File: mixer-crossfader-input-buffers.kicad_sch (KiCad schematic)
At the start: 21 parts, among them SW1701 SW_DIP_x02, U1701 TL072

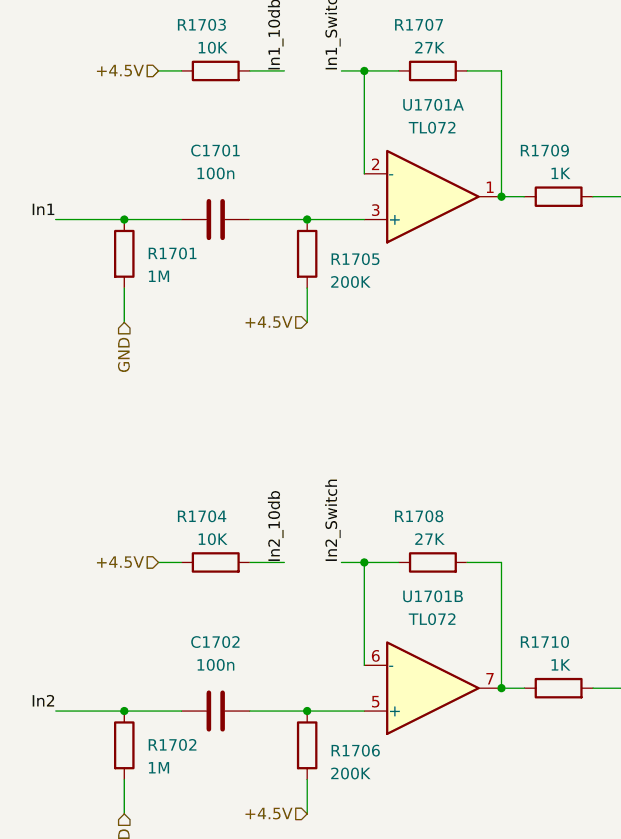
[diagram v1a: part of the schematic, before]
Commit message: Increase the size of dc blocking caps
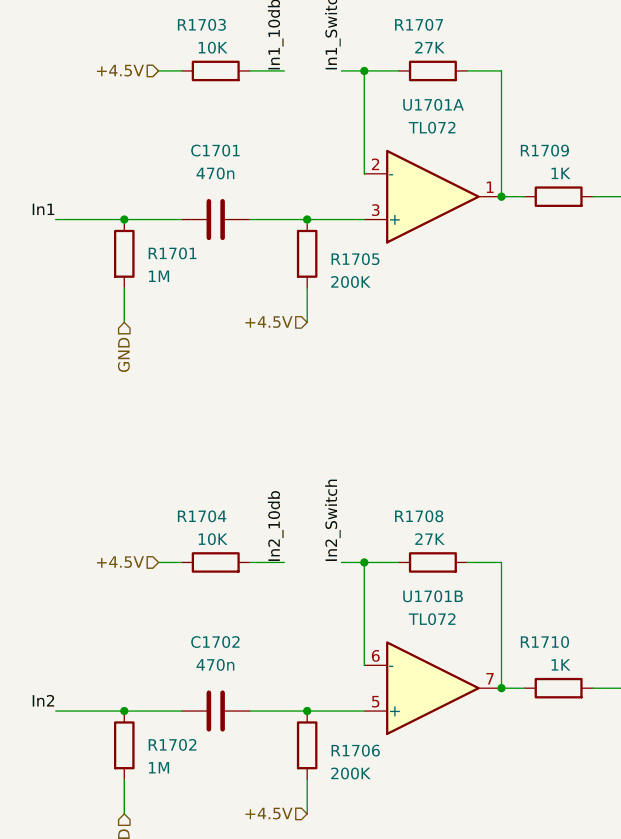
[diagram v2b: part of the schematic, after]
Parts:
- C1701, C1702: value 100n -> 470n; footprint Capacitor_SMD:C_0603_1608Metric_Pad1.08x0.95mm_HandSolder -> Capacitor_SMD:C_0805_2012Metric_Pad1.18x1.45mm_HandSolder
- C1703, C1704: footprint Capacitor_SMD:C_0603_1608Metric_Pad1.08x0.95mm_HandSolder -> Capacitor_SMD:C_0805_2012Metric_Pad1.18x1.45mm_HandSolder
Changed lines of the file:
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@@
-    (pin "2")
-  )
-  (symbol (lib_id "Device:C") (at 39.37 46.99 90) (unit 1)
-    (in_bom yes) (on_board yes) (fields_autoplaced)
-    (property "Reference" "C1701" (id 0) (at 39.37 39.37 90))
-    (property "Value" "100n" (id 1) (at 39.37 41.91 90))
-    (property "Footprint" "Capacitor_SMD:C_0603_1608Metric_Pad1.08x0.95mm_HandSolder" (id 2) (at 43.18 46.0248 0)
-      (effects (font (size 1.27 1.27)) hide)
-    )
-    (property "Datasheet" "~" (id 3) (at 39.37 46.99 0)
-      (effects (font (size 1.27 1.27)) hide)
-    )
-    (pin "1")
     (pin "2")
   )
@@
     (property "Reference" "C1703" (id 0) (at 88.9 36.83 90))
     (property "Value" "1u" (id 1) (at 88.9 39.37 90))
-    (property "Footprint" "Capacitor_SMD:C_0603_1608Metric_Pad1.08x0.95mm_HandSolder" (id 2) (at 92.71 43.4848 0)
+    (property "Footprint" "Capacitor_SMD:C_0805_2012Metric_Pad1.18x1.45mm_HandSolder" (id 2) (at 92.71 43.4848 0)
       (effects (font (size 1.27 1.27)) hide)
     )
@@
     (property "Reference" "C1704" (id 0) (at 88.9 91.44 90))
     (property "Value" "1u" (id 1) (at 88.9 93.98 90))
-    (property "Footprint" "Capacitor_SMD:C_0603_1608Metric_Pad1.08x0.95mm_HandSolder" (id 2) (at 92.71 98.0948 0)
+    (property "Footprint" "Capacitor_SMD:C_0805_2012Metric_Pad1.18x1.45mm_HandSolder" (id 2) (at 92.71 98.0948 0)
       (effects (font (size 1.27 1.27)) hide)
     )
@@
     )
     (property "Datasheet" "~" (id 3) (at 53.34 176.53 0)
+      (effects (font (size 1.27 1.27)) hide)
+    )
+    (pin "1")
+    (pin "2")
+  )
+  (symbol (lib_id "Device:C") (at 39.37 46.99 90) (unit 1)
+    (in_bom yes) (on_board yes) (fields_autoplaced)
+    (property "Reference" "C1701" (id 0) (at 39.37 39.37 90))
+    (property "Value" "470n" (id 1) (at 39.37 41.91 90))
+    (property "Footprint" "Capacitor_SMD:C_0805_2012Metric_Pad1.18x1.45mm_HandSolder" (id 2) (at 43.18 46.0248 0)
+      (effects (font (size 1.27 1.27)) hide)
+    )
+    (property "Datasheet" "~" (id 3) (at 39.37 46.99 0)
       (effects (font (size 1.27 1.27)) hide)
     )
@@
     (pin "2")
   )
-  (symbol (lib_id "Device:C") (at 39.37 101.6 90) (unit 1)
-    (in_bom yes) (on_board yes) (fields_autoplaced)
-    (property "Reference" "C1702" (id 0) (at 39.37 93.98 90))
-    (property "Value" "100n" (id 1) (at 39.37 96.52 90))
-    (property "Footprint" "Capacitor_SMD:C_0603_1608Metric_Pad1.08x0.95mm_HandSolder" (id 2) (at 43.18 100.6348 0)
-      (effects (font (size 1.27 1.27)) hide)
-    )
-    (property "Datasheet" "~" (id 3) (at 39.37 101.6 0)
-      (effects (font (size 1.27 1.27)) hide)
-    )
-    (pin "1")
-    (pin "2")
-  )
   (symbol (lib_id "Mechanical:MountingHole_Pad") (at 55.88 167.64 270) (unit 1)
     (in_bom yes) (on_board yes) (fields_autoplaced)
@@
     (pin "4")
   )
+  (symbol (lib_id "Device:C") (at 39.37 101.6 90) (unit 1)
+    (in_bom yes) (on_board yes) (fields_autoplaced)
+    (property "Reference" "C1702" (id 0) (at 39.37 93.98 90))
+    (property "Value" "470n" (id 1) (at 39.37 96.52 90))
+    (property "Footprint" "Capacitor_SMD:C_0805_2012Metric_Pad1.18x1.45mm_HandSolder" (id 2) (at 43.18 100.6348 0)
+      (effects (font (size 1.27 1.27)) hide)
+    )
+    (property "Datasheet" "~" (id 3) (at 39.37 101.6 0)
+      (effects (font (size 1.27 1.27)) hide)
+    )
+    (pin "1")
+    (pin "2")
+  )
   (symbol (lib_id "Amplifier_Operational:TL072") (at 252.73 46.99 0) (unit 3)

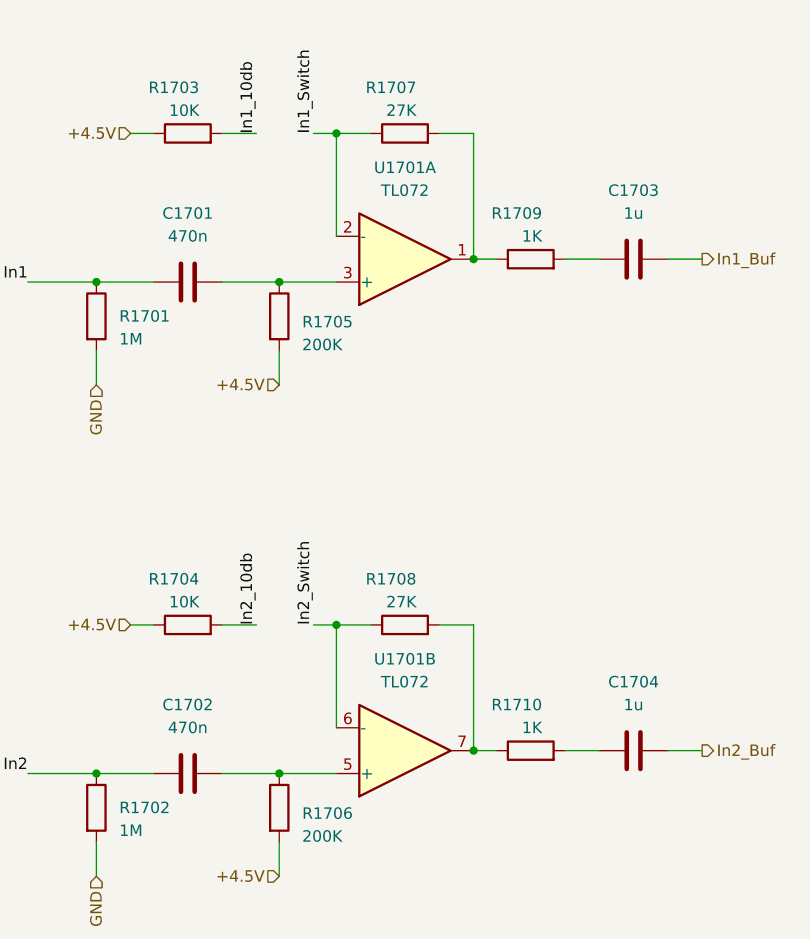
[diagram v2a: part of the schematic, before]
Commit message: Swap ins horizontaly on mixer
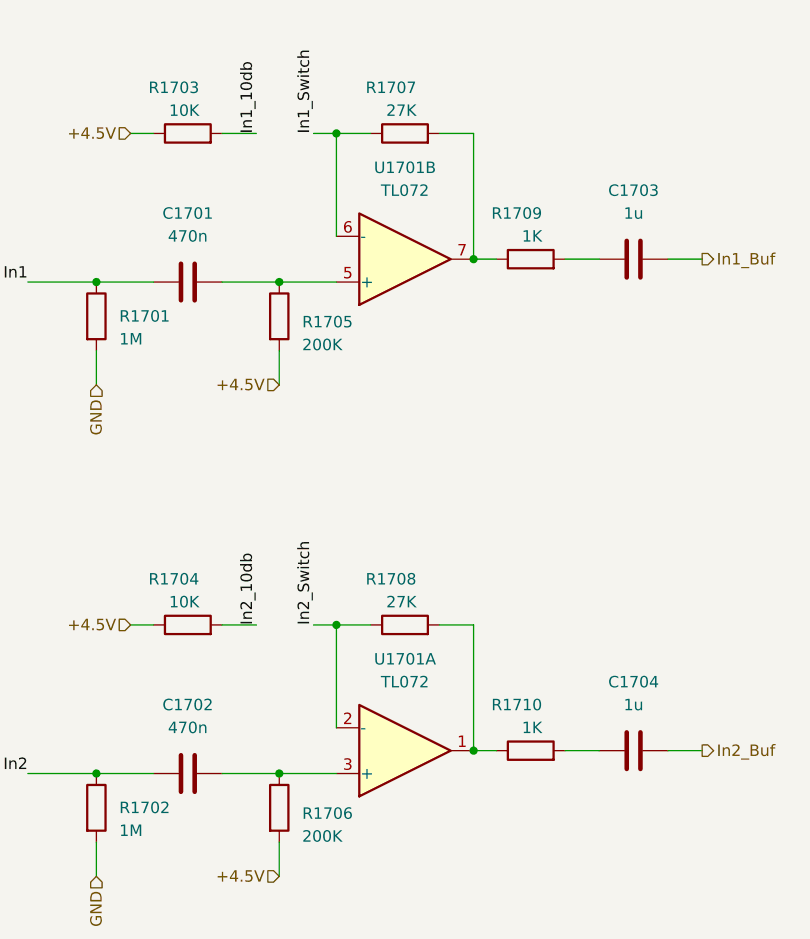
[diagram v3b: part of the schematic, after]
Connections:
- net In1_Switch: now also U1701.6 (-); no longer U1701.2 (-)
- net In2_Switch: now also U1701.2 (-); no longer U1701.6 (-)
- net at R1707.2, R1709.1: now also U1701.7; no longer U1701.1
- net at C1701.2, R1705.1: now also U1701.5 (+); no longer U1701.3 (+)
- net at R1708.2, R1710.1: now also U1701.1; no longer U1701.7
- net at C1702.2, R1706.1: now also U1701.3 (+); no longer U1701.5 (+)
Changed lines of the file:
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@@
     (pin "2")
   )
-  (symbol (lib_id "Amplifier_Operational:TL072") (at 63.5 44.45 0) (mirror x) (unit 1)
+  (symbol (lib_id "Amplifier_Operational:TL072") (at 63.5 44.45 0) (mirror x) (unit 2)
     (in_bom yes) (on_board yes) (fields_autoplaced)
     (property "Reference" "U1701" (id 0) (at 63.5 34.29 0))
@@
     (pin "2")
   )
-  (symbol (lib_id "Amplifier_Operational:TL072") (at 63.5 99.06 0) (mirror x) (unit 2)
+  (symbol (lib_id "Amplifier_Operational:TL072") (at 63.5 99.06 0) (mirror x) (unit 1)
     (in_bom yes) (on_board yes) (fields_autoplaced)
     (property "Reference" "U1701" (id 0) (at 63.5 88.9 0))

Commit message: Add JLC parts numbers
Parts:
- C1701, C1702: LCSC (none) -> C651004; Role (none) -> audio-coupling
- C1703, C1704: LCSC (none) -> C215803; Role (none) -> audio-coupling
- C1705: LCSC (none) -> C497032; Role (none) -> ic-bypass
- D1701, D1702: LCSC (none) -> C20936
- R1701, R1702: LCSC (none) -> C234360
- R1703, R1704: LCSC (none) -> C98220
- R1705, R1706: LCSC (none) -> C203392
- R1707, R1708: LCSC (none) -> C116691
- R1709, R1710: LCSC (none) -> C2907002
- U1701: LCSC (none) -> C67473
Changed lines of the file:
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@@
+      (effects (font (size 1.27 1.27)) hide)
+    )
+    (property "LCSC" "C234360" (id 4) (at 29.21 105.41 0)
       (effects (font (size 1.27 1.27)) hide)
     )
@@
     )
     (property "Datasheet" "~" (id 3) (at 29.21 176.53 0)
+      (effects (font (size 1.27 1.27)) hide)
+    )
+    (property "LCSC" "C20936" (id 4) (at 29.21 176.53 0)
       (effects (font (size 1.27 1.27)) hide)
     )
@@
     )
     (property "Datasheet" "http://www.ti.com/lit/ds/symlink/tl071.pdf" (id 3) (at 63.5 44.45 0)
+      (effects (font (size 1.27 1.27)) hide)
+    )
+    (property "LCSC" "C67473" (id 4) (at 63.5 44.45 0)
       (effects (font (size 1.27 1.27)) hide)
     )
@@
       (effects (font (size 1.27 1.27)) hide)
     )
+    (property "LCSC" "C116691" (id 4) (at 63.5 85.09 0)
+      (effects (font (size 1.27 1.27)) hide)
+    )
     (pin "1")
     (pin "2")
@@
       (effects (font (size 1.27 1.27)) hide)
     )
+    (property "LCSC" "C215803" (id 4) (at 88.9 44.45 0)
+      (effects (font (size 1.27 1.27)) hide)
+    )
+    (property "Role" "audio-coupling" (id 5) (at 88.9 44.45 0)
+      (effects (font (size 1.27 1.27)) hide)
+    )
     (pin "1")
     (pin "2")
@@
     )
     (property "Datasheet" "~" (id 3) (at 39.37 85.09 0)
+      (effects (font (size 1.27 1.27)) hide)
+    )
+    (property "LCSC" "C98220" (id 4) (at 39.37 85.09 0)
       (effects (font (size 1.27 1.27)) hide)
     )
@@
       (effects (font (size 1.27 1.27)) hide)
     )
+    (property "LCSC" "C215803" (id 4) (at 88.9 99.06 0)
+      (effects (font (size 1.27 1.27)) hide)
+    )
+    (property "Role" "audio-coupling" (id 5) (at 88.9 99.06 0)
+      (effects (font (size 1.27 1.27)) hide)
+    )
     (pin "1")
     (pin "2")
@@
       (effects (font (size 1.27 1.27)) hide)
     )
+    (property "LCSC" "C2907002" (id 4) (at 77.47 44.45 0)
+      (effects (font (size 1.27 1.27)) hide)
+    )
     (pin "1")
     (pin "2")
@@
     )
     (property "Datasheet" "~" (id 3) (at 49.53 105.41 0)
+      (effects (font (size 1.27 1.27)) hide)
+    )
+    (property "LCSC" "C203392" (id 4) (at 49.53 105.41 0)
       (effects (font (size 1.27 1.27)) hide)
     )
@@
     )
     (property "Datasheet" "~" (id 3) (at 53.34 176.53 0)
+      (effects (font (size 1.27 1.27)) hide)
+    )
+    (property "LCSC" "C20936" (id 4) (at 53.34 176.53 0)
       (effects (font (size 1.27 1.27)) hide)
     )
@@
       (effects (font (size 1.27 1.27)) hide)
     )
+    (property "LCSC" "C651004" (id 4) (at 39.37 46.99 0)
+      (effects (font (size 1.27 1.27)) hide)
+    )
+    (property "Role" "audio-coupling" (id 5) (at 39.37 46.99 0)
+      (effects (font (size 1.27 1.27)) hide)
+    )
     (pin "1")
     (pin "2")
@@
     )
     (property "Datasheet" "http://www.ti.com/lit/ds/symlink/tl071.pdf" (id 3) (at 63.5 99.06 0)
+      (effects (font (size 1.27 1.27)) hide)
+    )
+    (property "LCSC" "C67473" (id 4) (at 63.5 99.06 0)
       (effects (font (size 1.27 1.27)) hide)
     )
@@
       (effects (font (size 1.27 1.27)) hide)
     )
+    (property "LCSC" "C116691" (id 4) (at 63.5 30.48 0)
+      (effects (font (size 1.27 1.27)) hide)
+    )
     (pin "1")
     (pin "2")
@@
       (effects (font (size 1.27 1.27)) hide)
     )
+    (property "LCSC" "C98220" (id 4) (at 39.37 30.48 0)
+      (effects (font (size 1.27 1.27)) hide)
+    )
     (pin "1")
     (pin "2")
@@
       (effects (font (size 1.27 1.27)) hide)
     )
+    (property "LCSC" "C497032" (id 4) (at 238.76 46.99 0)
+      (effects (font (size 1.27 1.27)) hide)
+    )
+    (property "Role" "ic-bypass" (id 5) (at 238.76 46.99 0)
+      (effects (font (size 1.27 1.27)) hide)
+    )
     (pin "1")
     (pin "2")
@@
       (effects (font (size 1.27 1.27)) hide)
     )
+    (property "LCSC" "C2907002" (id 4) (at 77.47 99.06 0)
+      (effects (font (size 1.27 1.27)) hide)
+    )
     (pin "1")
     (pin "2")
@@
     )
     (property "Datasheet" "~" (id 3) (at 49.53 50.8 0)
+      (effects (font (size 1.27 1.27)) hide)
+    )
+    (property "LCSC" "C203392" (id 4) (at 49.53 50.8 0)
       (effects (font (size 1.27 1.27)) hide)
     )
@@
       (effects (font (size 1.27 1.27)) hide)
     )
+    (property "LCSC" "C651004" (id 4) (at 39.37 101.6 0)
+      (effects (font (size 1.27 1.27)) hide)
+    )
+    (property "Role" "audio-coupling" (id 5) (at 39.37 101.6 0)
+      (effects (font (size 1.27 1.27)) hide)
+    )
     (pin "1")
     (pin "2")
@@
     )
     (property "Datasheet" "http://www.ti.com/lit/ds/symlink/tl071.pdf" (id 3) (at 252.73 46.99 0)
+      (effects (font (size 1.27 1.27)) hide)
+    )
+    (property "LCSC" "C67473" (id 4) (at 252.73 46.99 0)
       (effects (font (size 1.27 1.27)) hide)
     )
@@
       (effects (font (size 1.27 1.27)) hide)
     )
+    (property "LCSC" "C234360" (id 4) (at 29.21 50.8 0)
+      (effects (font (size 1.27 1.27)) hide)
+    )
